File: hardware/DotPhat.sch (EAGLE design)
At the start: 31 parts, among them CN1 1X4-BIG, IC1 CAT24M010TS, J2 RASPBERRYPI-40-PIN-GPIO_PTH, J3 USB-MICROB, U1 ATMEGA328P-MU-QFN32, U2 TMP102, U3 ATSHA204-TSU, X3 S4B-ZR

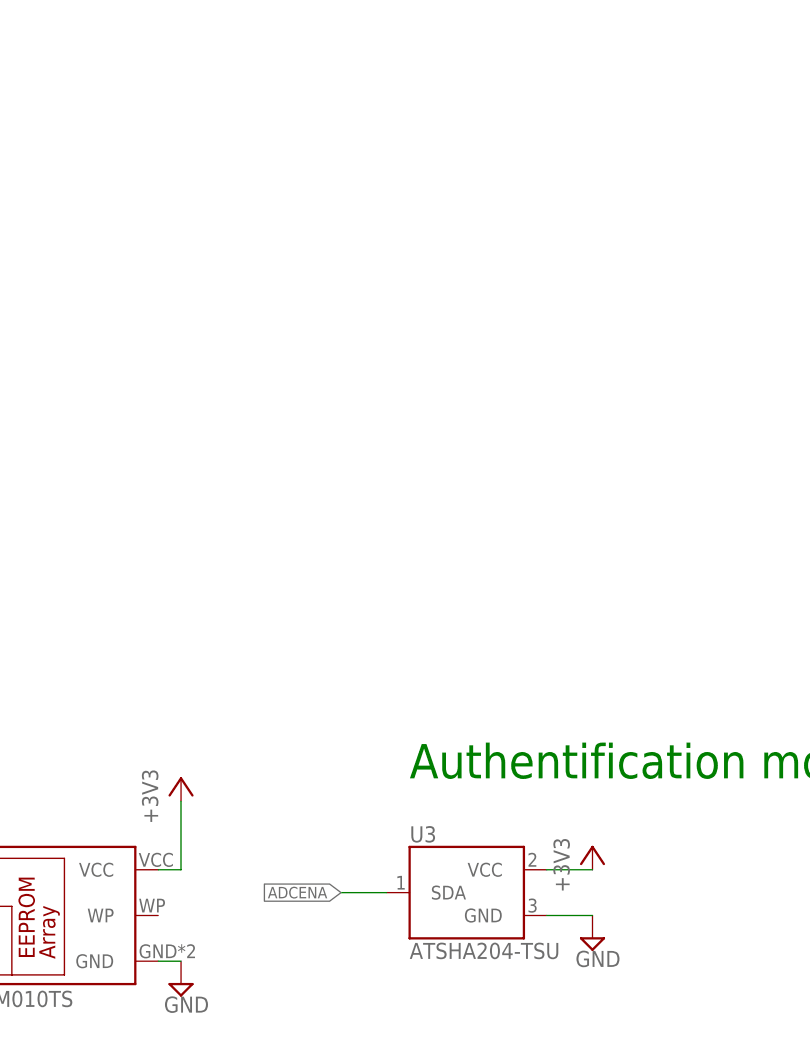
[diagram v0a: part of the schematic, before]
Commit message: Add pullup on SDA for crypto & bypass cap
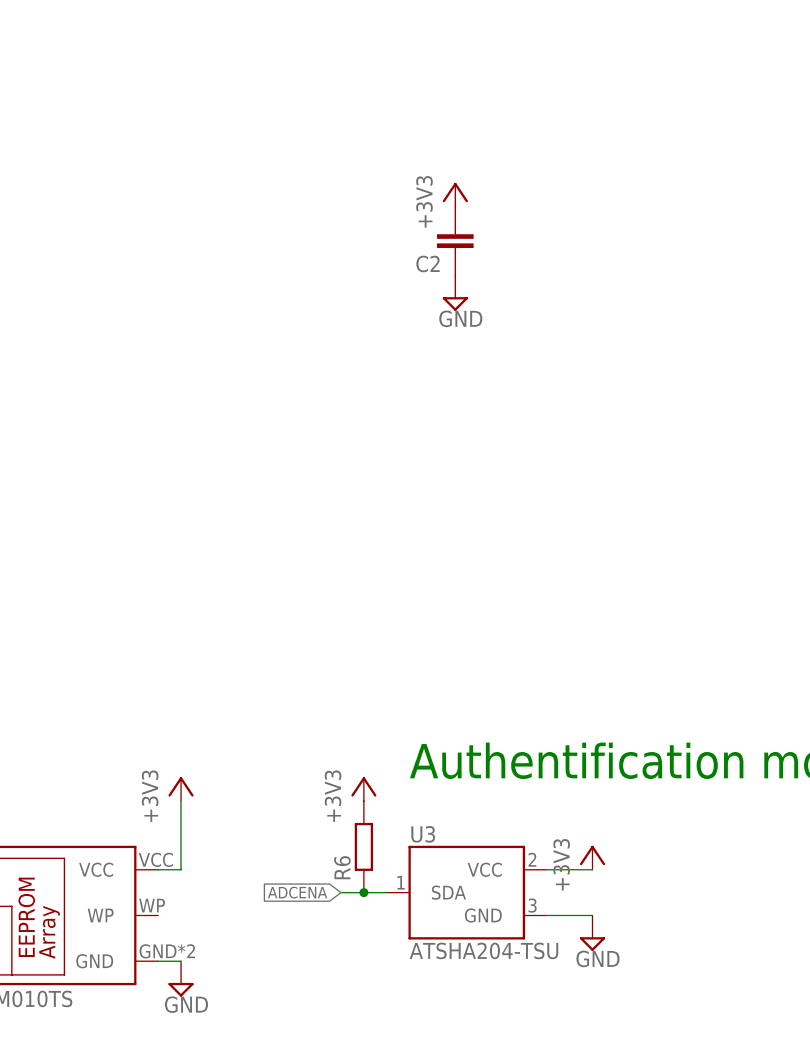
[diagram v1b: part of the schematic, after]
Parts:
- added C2: (no value), rcl:C-EUC3216
- added R6: (no value), rcl:R-EU_R0603
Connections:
- net +3V3: now also C2.2, R6.2
- net ADCENA: now also R6.1
- net GND: now also C2.1
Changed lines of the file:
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@@
 <part name="+3V10" library="supply1" deviceset="+3V3" device=""/>
 <part name="SUPPLY18" library="supply2" deviceset="GND" device=""/>
+<part name="R6" library="rcl" deviceset="R-EU_" device="R0603"/>
+<part name="+3V13" library="supply1" deviceset="+3V3" device=""/>
+<part name="C2" library="rcl" deviceset="C-EU" device="C3216"/>
+<part name="+3V15" library="supply1" deviceset="+3V3" device=""/>
+<part name="SUPPLY20" library="supply2" deviceset="GND" device=""/>
 </parts>
 <sheets>
@@
 <instance part="+3V10" gate="G$1" x="157.48" y="-154.94"/>
 <instance part="SUPPLY18" gate="GND" x="157.48" y="-165.1"/>
+<instance part="R6" gate="G$1" x="132.08" y="-154.94" rot="R90"/>
+<instance part="+3V13" gate="G$1" x="132.08" y="-147.32"/>
+<instance part="C2" gate="G$1" x="142.24" y="-88.9" rot="R180"/>
+<instance part="+3V15" gate="G$1" x="142.24" y="-81.28"/>
+<instance part="SUPPLY20" gate="GND" x="142.24" y="-93.98"/>
 </instances>
 <busses>
@@
 <pinref part="SUPPLY18" gate="GND" pin="GND"/>
 </segment>
+<segment>
+<pinref part="C2" gate="G$1" pin="1"/>
+<pinref part="SUPPLY20" gate="GND" pin="GND"/>
+</segment>
 </net>
 <net name="SDA" class="0">
@@
 <pinref part="+3V10" gate="G$1" pin="+3V3"/>
 </segment>
+<segment>
+<pinref part="R6" gate="G$1" pin="2"/>
+<pinref part="+3V13" gate="G$1" pin="+3V3"/>
+</segment>
+<segment>
+<pinref part="C2" gate="G$1" pin="2"/>
+<pinref part="+3V15" gate="G$1" pin="+3V3"/>
+</segment>
 </net>
 <net name="ADCENA" class="0">
@@
 <segment>
 <pinref part="U3" gate="G$1" pin="SDA"/>
-<wire x1="134.62" y1="-160.02" x2="129.54" y2="-160.02" width="0.1524" layer="91"/>
+<wire x1="134.62" y1="-160.02" x2="132.08" y2="-160.02" width="0.1524" layer="91"/>
 <label x="129.54" y="-160.02" size="1.27" layer="95" rot="R180" xref="yes"/>
-</segment>
-</net>
+<pinref part="R6" gate="G$1" pin="1"/>
+<wire x1="132.08" y1="-160.02" x2="129.54" y2="-160.02" width="0.1524" layer="91"/>
+<junction x="132.08" y="-160.02"/>
+</segment>
+</net>

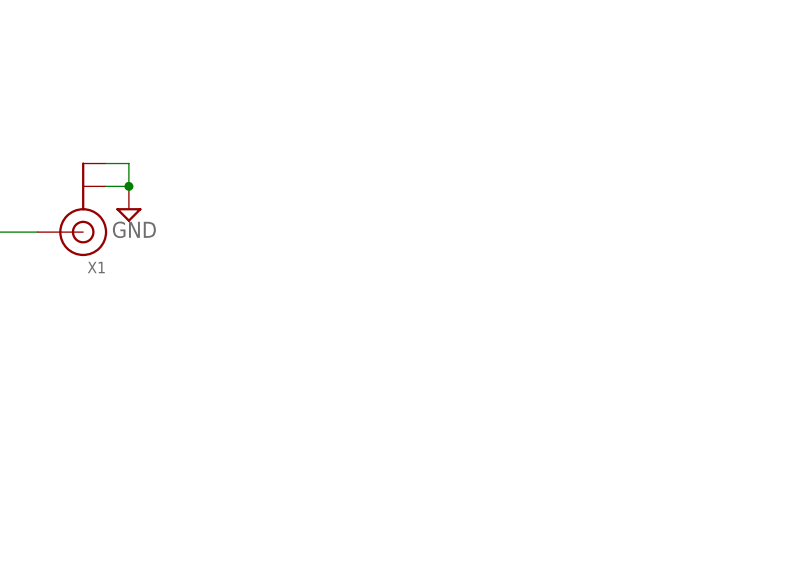
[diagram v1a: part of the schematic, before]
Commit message: Add Pi-network for antenna matching
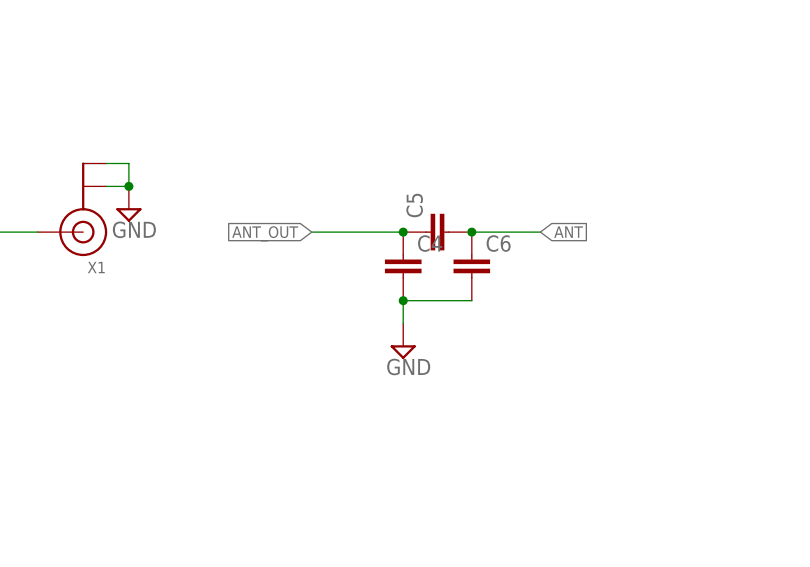
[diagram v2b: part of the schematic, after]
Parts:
- added C4, C5, C6: (no value), rcl:C-EUC0603
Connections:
- removed net N$3: U$1.ANT, X1.SIGNAL
- new net ANT: C5.2, C6.1
- new net ANT_OUT: C4.1, C5.1, U$1.ANT, X1.SIGNAL
- net GND: now also C4.2, C6.2
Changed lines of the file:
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@@
 <part name="+3V15" library="supply1" deviceset="+3V3" device=""/>
 <part name="SUPPLY20" library="supply2" deviceset="GND" device=""/>
+<part name="C4" library="rcl" deviceset="C-EU" device="C0603"/>
+<part name="C5" library="rcl" deviceset="C-EU" device="C0603"/>
+<part name="C6" library="rcl" deviceset="C-EU" device="C0603"/>
+<part name="SUPPLY21" library="supply2" deviceset="GND" device=""/>
 </parts>
 <sheets>
@@
 <instance part="+3V15" gate="G$1" x="142.24" y="-81.28"/>
 <instance part="SUPPLY20" gate="GND" x="142.24" y="-93.98"/>
+<instance part="C4" gate="G$1" x="213.36" y="68.58"/>
+<instance part="C5" gate="G$1" x="215.9" y="71.12" rot="R90"/>
+<instance part="C6" gate="G$1" x="220.98" y="68.58"/>
+<instance part="SUPPLY21" gate="GND" x="213.36" y="58.42"/>
 </instances>
 <busses>
@@
 <pinref part="SUPPLY20" gate="GND" pin="GND"/>
 </segment>
+<segment>
+<pinref part="C4" gate="G$1" pin="2"/>
+<pinref part="SUPPLY21" gate="GND" pin="GND"/>
+<wire x1="213.36" y1="63.5" x2="213.36" y2="60.96" width="0.1524" layer="91"/>
+<pinref part="C6" gate="G$1" pin="2"/>
+<wire x1="220.98" y1="63.5" x2="213.36" y2="63.5" width="0.1524" layer="91"/>
+<junction x="213.36" y="63.5"/>
+</segment>
 </net>
 <net name="SDA" class="0">
@@
 </segment>
 </net>
-<net name="N$3" class="0">
-<segment>
-<pinref part="U$1" gate="G$1" pin="ANT"/>
-<pinref part="X1" gate="G$1" pin="SIGNAL"/>
-<wire x1="157.48" y1="71.12" x2="172.72" y2="71.12" width="0.1524" layer="91"/>
-</segment>
-</net>
 <net name="OUTA" class="0">
 <segment>
@@
 </segment>
 </net>
+<net name="ANT_OUT" class="0">
+<segment>
+<pinref part="C4" gate="G$1" pin="1"/>
+<pinref part="C5" gate="G$1" pin="1"/>
+<wire x1="213.36" y1="71.12" x2="203.2" y2="71.12" width="0.1524" layer="91"/>
+<junction x="213.36" y="71.12"/>
+<label x="203.2" y="71.12" size="1.27" layer="95" rot="R180" xref="yes"/>
+</segment>
+<segment>
+<pinref part="U$1" gate="G$1" pin="ANT"/>
+<pinref part="X1" gate="G$1" pin="SIGNAL"/>
+<wire x1="157.48" y1="71.12" x2="172.72" y2="71.12" width="0.1524" layer="91"/>
+</segment>
+</net>
+<net name="ANT" class="0">
+<segment>
+<pinref part="C5" gate="G$1" pin="2"/>
+<pinref part="C6" gate="G$1" pin="1"/>
+<wire x1="220.98" y1="71.12" x2="228.6" y2="71.12" width="0.1524" layer="91"/>
+<junction x="220.98" y="71.12"/>
+<label x="228.6" y="71.12" size="1.27" layer="95" xref="yes"/>
+</segment>
+</net>

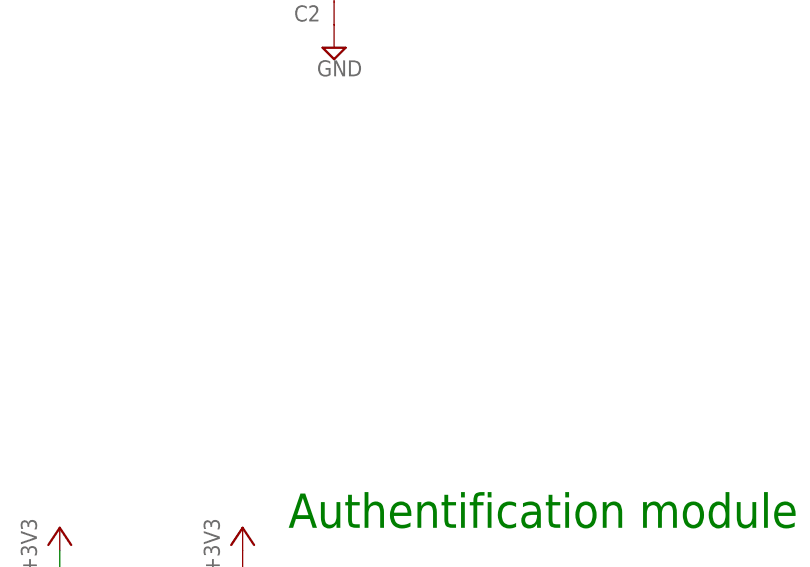
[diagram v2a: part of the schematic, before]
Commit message: Add support for high-precision chrystal
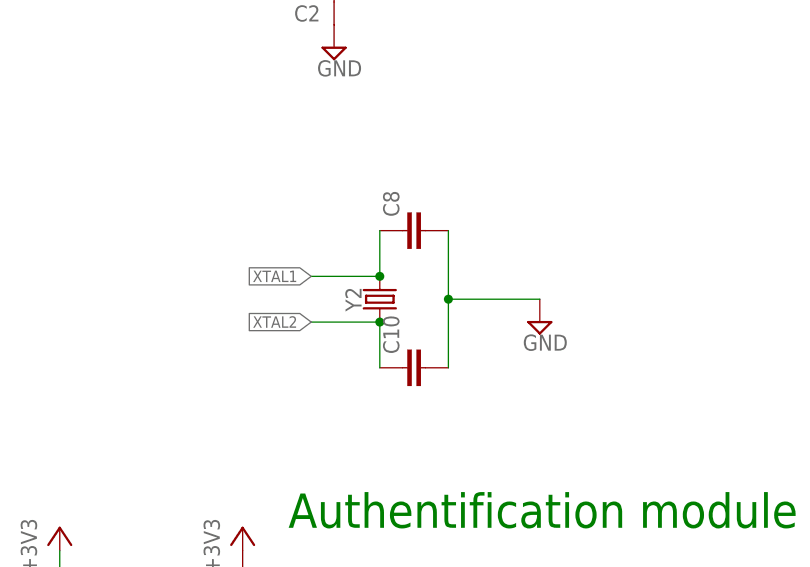
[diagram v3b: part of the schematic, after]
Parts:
- added C10, C8: (no value), rcl:C-EUC0402
- added Y2: (no value), SparkFun-Clocks:CRYSTALSMD-3.2X1.5
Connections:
- new net XTAL1: C8.1, Y2.2
- new net XTAL2: C10.1, Y2.1
- net GND: now also C10.2, C8.2
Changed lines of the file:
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@@
 <part name="C6" library="rcl" deviceset="C-EU" device="C0603"/>
 <part name="SUPPLY21" library="supply2" deviceset="GND" device=""/>
+<part name="Y2" library="SparkFun-Clocks" deviceset="CRYSTAL" device="SMD-3.2X1.5"/>
+<part name="SUPPLY26" library="supply2" deviceset="GND" device=""/>
+<part name="C8" library="rcl" deviceset="C-EU" device="C0402"/>
+<part name="C10" library="rcl" deviceset="C-EU" device="C0402"/>
 </parts>
 <sheets>
@@
 <instance part="C6" gate="G$1" x="220.98" y="68.58"/>
 <instance part="SUPPLY21" gate="GND" x="213.36" y="58.42"/>
+<instance part="Y2" gate="G$1" x="147.32" y="-121.92" rot="R90"/>
+<instance part="SUPPLY26" gate="GND" x="165.1" y="-124.46"/>
+<instance part="C8" gate="G$1" x="149.86" y="-114.3" rot="R90"/>
+<instance part="C10" gate="G$1" x="149.86" y="-129.54" rot="R90"/>
 </instances>
 <busses>
@@
 <junction x="213.36" y="63.5"/>
 </segment>
+<segment>
+<wire x1="154.94" y1="-114.3" x2="154.94" y2="-121.92" width="0.1524" layer="91"/>
+<pinref part="SUPPLY26" gate="GND" pin="GND"/>
+<wire x1="154.94" y1="-121.92" x2="154.94" y2="-129.54" width="0.1524" layer="91"/>
+<wire x1="165.1" y1="-121.92" x2="154.94" y2="-121.92" width="0.1524" layer="91"/>
+<junction x="154.94" y="-121.92"/>
+<pinref part="C8" gate="G$1" pin="2"/>
+<pinref part="C10" gate="G$1" pin="2"/>
+</segment>
 </net>
 <net name="SDA" class="0">
@@
 </segment>
 </net>
+<net name="XTAL1" class="0">
+<segment>
+<pinref part="Y2" gate="G$1" pin="2"/>
+<wire x1="147.32" y1="-114.3" x2="147.32" y2="-119.38" width="0.1524" layer="91"/>
+<wire x1="147.32" y1="-119.38" x2="139.7" y2="-119.38" width="0.1524" layer="91"/>
+<junction x="147.32" y="-119.38"/>
+<label x="139.7" y="-119.38" size="1.27" layer="95" rot="R180" xref="yes"/>
+<pinref part="C8" gate="G$1" pin="1"/>
+</segment>
+</net>
+<net name="XTAL2" class="0">
+<segment>
+<pinref part="Y2" gate="G$1" pin="1"/>
+<wire x1="147.32" y1="-124.46" x2="147.32" y2="-129.54" width="0.1524" layer="91"/>
+<wire x1="147.32" y1="-124.46" x2="139.7" y2="-124.46" width="0.1524" layer="91"/>
+<junction x="147.32" y="-124.46"/>
+<label x="139.7" y="-124.46" size="1.27" layer="95" rot="R180" xref="yes"/>
+<pinref part="C10" gate="G$1" pin="1"/>
+</segment>
+</net>

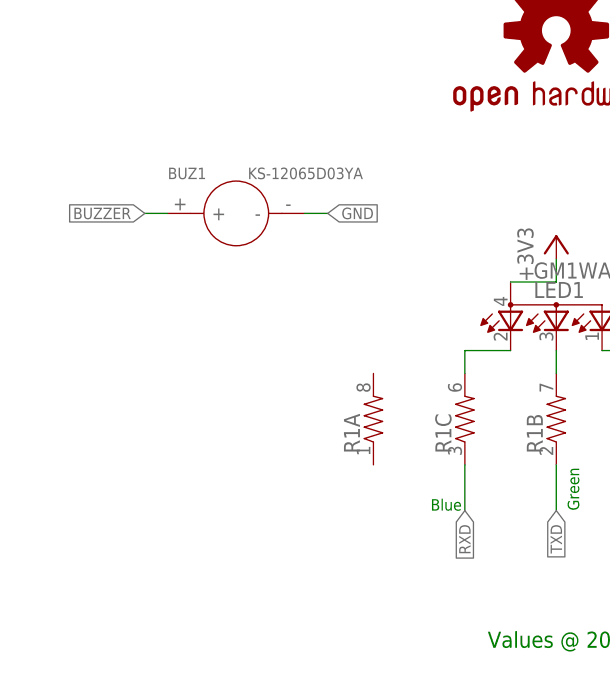
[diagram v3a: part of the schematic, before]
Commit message: Switch to SMD buzzer
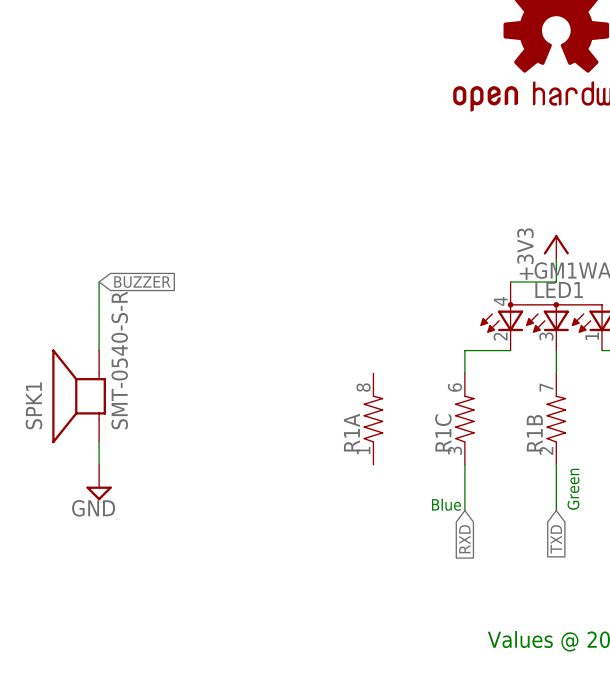
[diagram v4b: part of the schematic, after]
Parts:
- removed BUZ1: KS-12065D03YA, Seeed-OPL-Connector:DIP-BUZZER-3V(KS-12065D03YA)
- added SPK1: SMT-0540-S-R, adafruit:SMT-0540-S-R
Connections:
- net BUZZER: now also SPK1.-; no longer BUZ1.+
- net GND: now also SPK1.+; no longer BUZ1.-
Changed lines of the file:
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@@
 <part name="LED1" library="led" deviceset="GM1WA55311A" device=""/>
 <part name="J2" library="SparkFun-Connectors" deviceset="RASPBERRYPI-40-PIN-GPIO" device="_PTH"/>
-<part name="BUZ1" library="Seeed-OPL-Connector" deviceset="DIP-BUZZER-3V(KS-12065D03YA)" device="" value="KS-12065D03YA"/>
 <part name="LOGO1" library="Spark" deviceset="OSHW-LOGO" device="S"/>
 <part name="SUPPLY29" library="supply2" deviceset="GND" device=""/>
@@
 <part name="C8" library="rcl" deviceset="C-EU" device="C0402"/>
 <part name="C10" library="rcl" deviceset="C-EU" device="C0402"/>
+<part name="SPK1" library="adafruit" deviceset="SMT-0540-S-R" device=""/>
+<part name="SUPPLY22" library="supply2" deviceset="GND" device=""/>
 </parts>
 <sheets>
@@
 <instance part="LED1" gate="G$1" x="-22.86" y="73.66"/>
 <instance part="J2" gate="G$1" x="2.54" y="-30.48"/>
-<instance part="BUZ1" gate="G$1" x="-58.42" y="83.82"/>
 <instance part="LOGO1" gate="G$1" x="-22.86" y="104.14"/>
 <instance part="SUPPLY29" gate="GND" x="160.02" y="142.24" rot="R90"/>
@@
 <instance part="C8" gate="G$1" x="149.86" y="-114.3" rot="R90"/>
 <instance part="C10" gate="G$1" x="149.86" y="-129.54" rot="R90"/>
+<instance part="SPK1" gate="G$1" x="-73.66" y="63.5" rot="R90"/>
+<instance part="SUPPLY22" gate="GND" x="-73.66" y="53.34" rot="MR0"/>
 </instances>
 <busses>
@@
 <pinref part="Y1" gate="G$1" pin="2"/>
 <pinref part="SUPPLY30" gate="GND" pin="GND"/>
-</segment>
-<segment>
-<pinref part="BUZ1" gate="G$1" pin="-"/>
-<wire x1="-50.8" y1="83.82" x2="-48.26" y2="83.82" width="0.1524" layer="91"/>
-<label x="-48.26" y="83.82" size="1.27" layer="95" xref="yes"/>
 </segment>
 <segment>
@@
 <pinref part="C10" gate="G$1" pin="2"/>
 </segment>
+<segment>
+<pinref part="SPK1" gate="G$1" pin="+"/>
+<wire x1="-73.66" y1="58.42" x2="-73.66" y2="55.88" width="0.1524" layer="91"/>
+<pinref part="SUPPLY22" gate="GND" pin="GND"/>
+</segment>
 </net>
 <net name="SDA" class="0">
@@
 </segment>
 <segment>
-<pinref part="BUZ1" gate="G$1" pin="+"/>
-<wire x1="-66.04" y1="83.82" x2="-68.58" y2="83.82" width="0.1524" layer="91"/>
-<label x="-68.58" y="83.82" size="1.27" layer="95" rot="R180" xref="yes"/>
-</segment>
-</net>
+<pinref part="SPK1" gate="G$1" pin="-"/>
+<wire x1="-73.66" y1="68.58" x2="-73.66" y2="76.2" width="0.1524" layer="91"/>
+<label x="-73.66" y="76.2" size="1.27" layer="95" xref="yes"/>
+</segment>
+</net>
